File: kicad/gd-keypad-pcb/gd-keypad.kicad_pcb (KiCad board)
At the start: 2 copper layers, 155 x 70 mm, 61 parts, among them J2 USB_C_Receptacle_USB2.0_16P, J3 TC2030, SW1 TS-1187A-B-A-B, SW2 TS-1187A-B-A-B, SW3 RotaryEncoder_Switch_MP, U1 AT32F405RCT7, U2 USBLC6-2SC6, U3 TLV75733PDBV, U4 XC6206P332MR-G, U5 SW_MX_HE, U6 SW_MX_HE, U7 SW_MX_HE, Y1 X322512MSB4SI

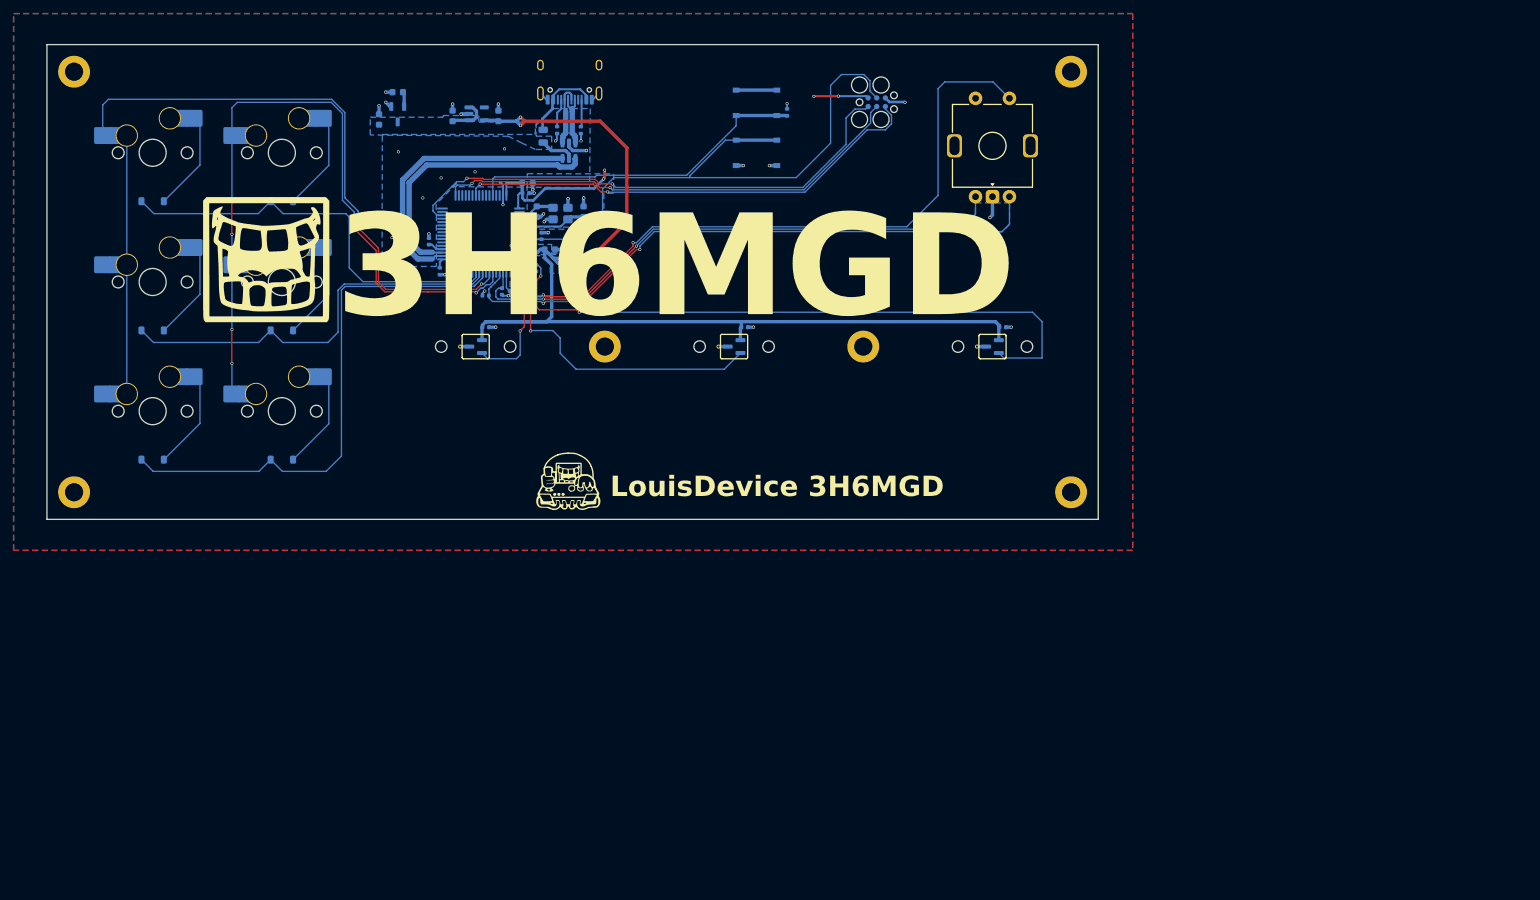
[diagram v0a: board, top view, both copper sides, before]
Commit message: update pcb dimension labels and 3d models visibility
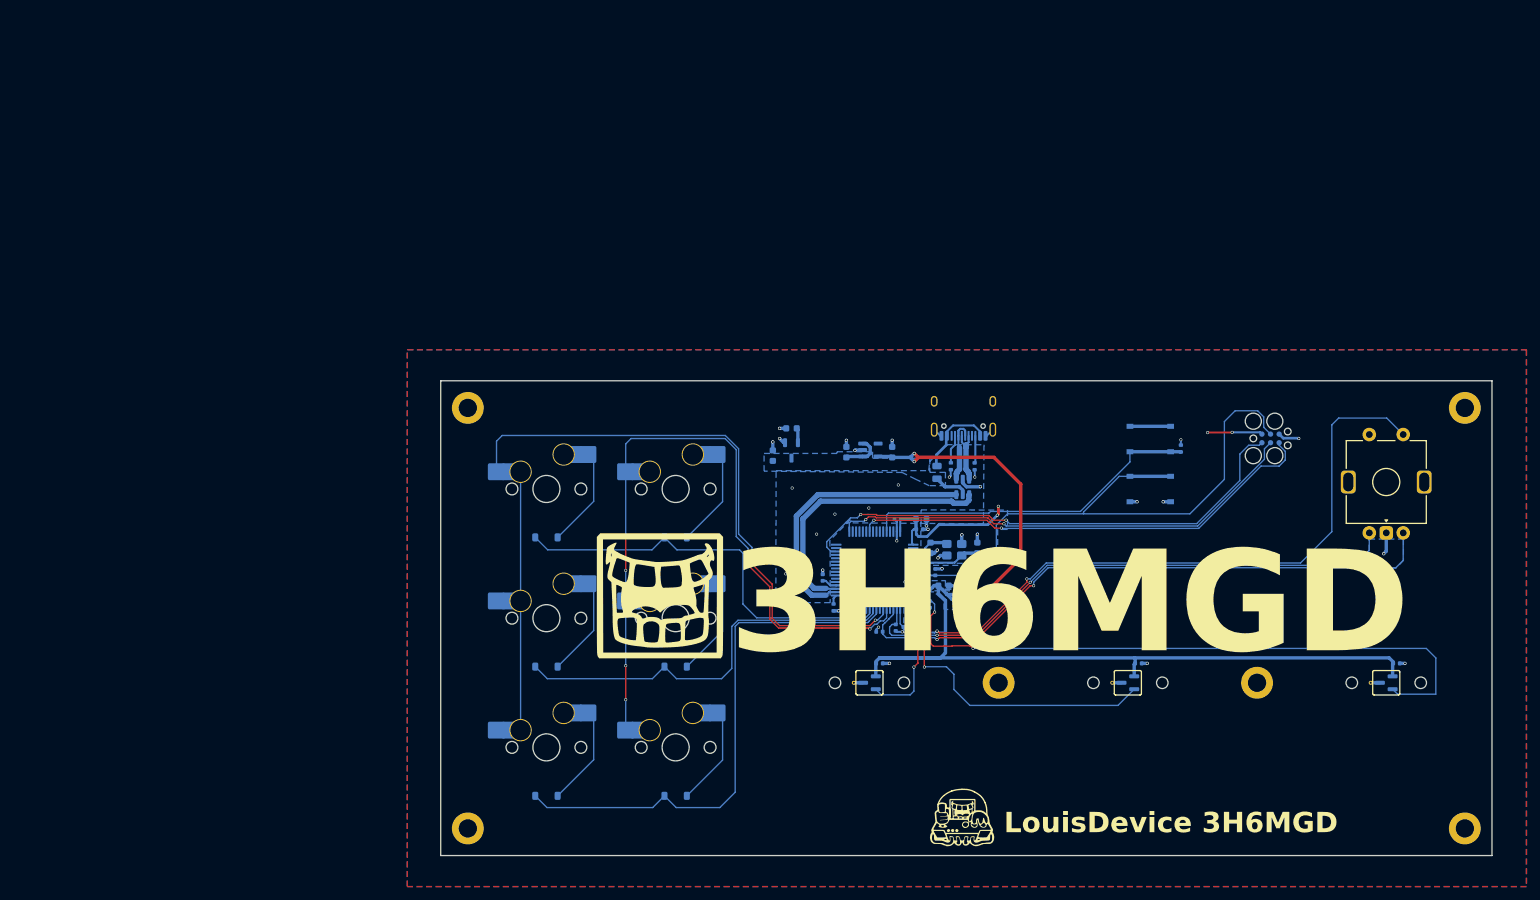
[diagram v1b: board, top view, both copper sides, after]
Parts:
- moved C150 76.3 mm to (121.0, 74.2)
- moved C151 76.3 mm to (123.7, 70.2)
- moved C155 76.3 mm to (128.3, 92.2)
- moved C156 76.3 mm to (139.4, 83.5)
- moved C158 76.3 mm to (143.7, 93.4)
- moved C159 76.3 mm to (146.1, 93.4)
- moved C160 76.3 mm to (144.9, 91.4)
- moved C2 76.3 mm to (140.8, 97.4)
- moved C5 76.3 mm to (212.9, 104.8)
- moved D6 76.3 mm to (106.6, 124.3)
- moved G*** 76.3 mm to (148.9, 126.0)
- moved G*** 76.3 mm to (104.3, 94.6)
- moved H5 76.3 mm to (154.3, 107.7)
- moved J2 76.3 mm to (149.1, 67.2)
- moved MX2 76.3 mm to (106.6, 79.1)
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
